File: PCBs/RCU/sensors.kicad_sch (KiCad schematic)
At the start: 10 parts

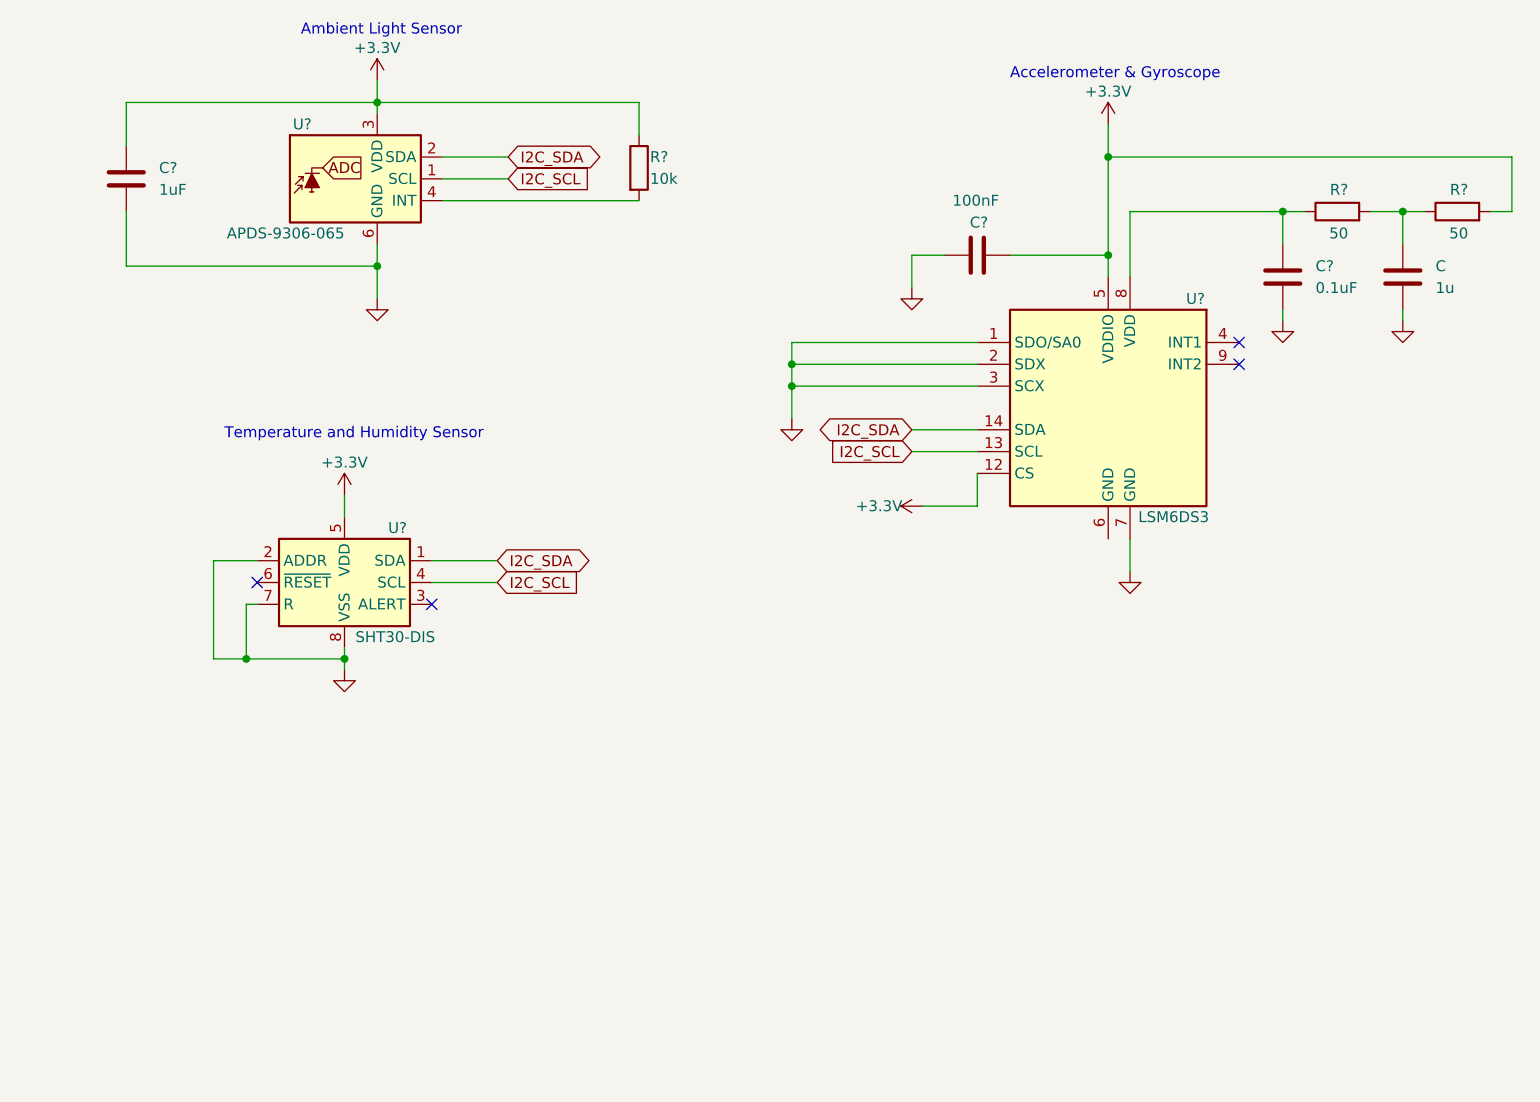
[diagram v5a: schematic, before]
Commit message: Numbered and ordered all of the modules
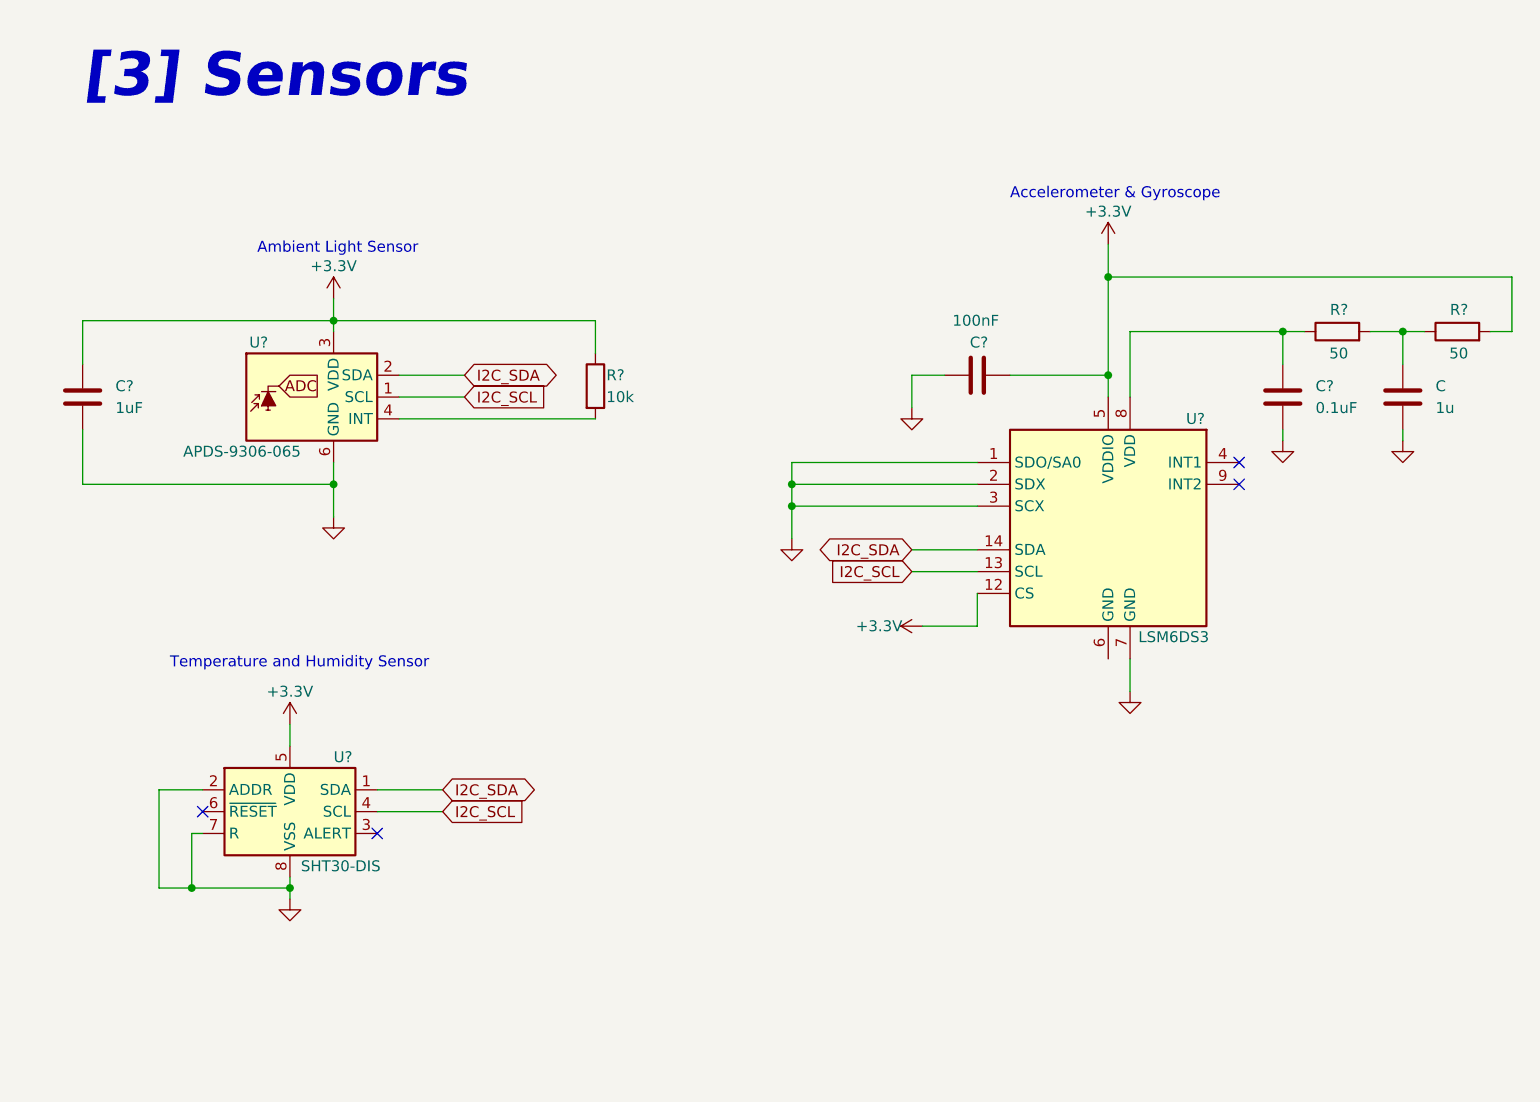
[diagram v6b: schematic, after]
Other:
- note added: "[3] Sensors"
- moved on the sheet: C, C?, R?, U?

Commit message: Annotated all components in sensors module
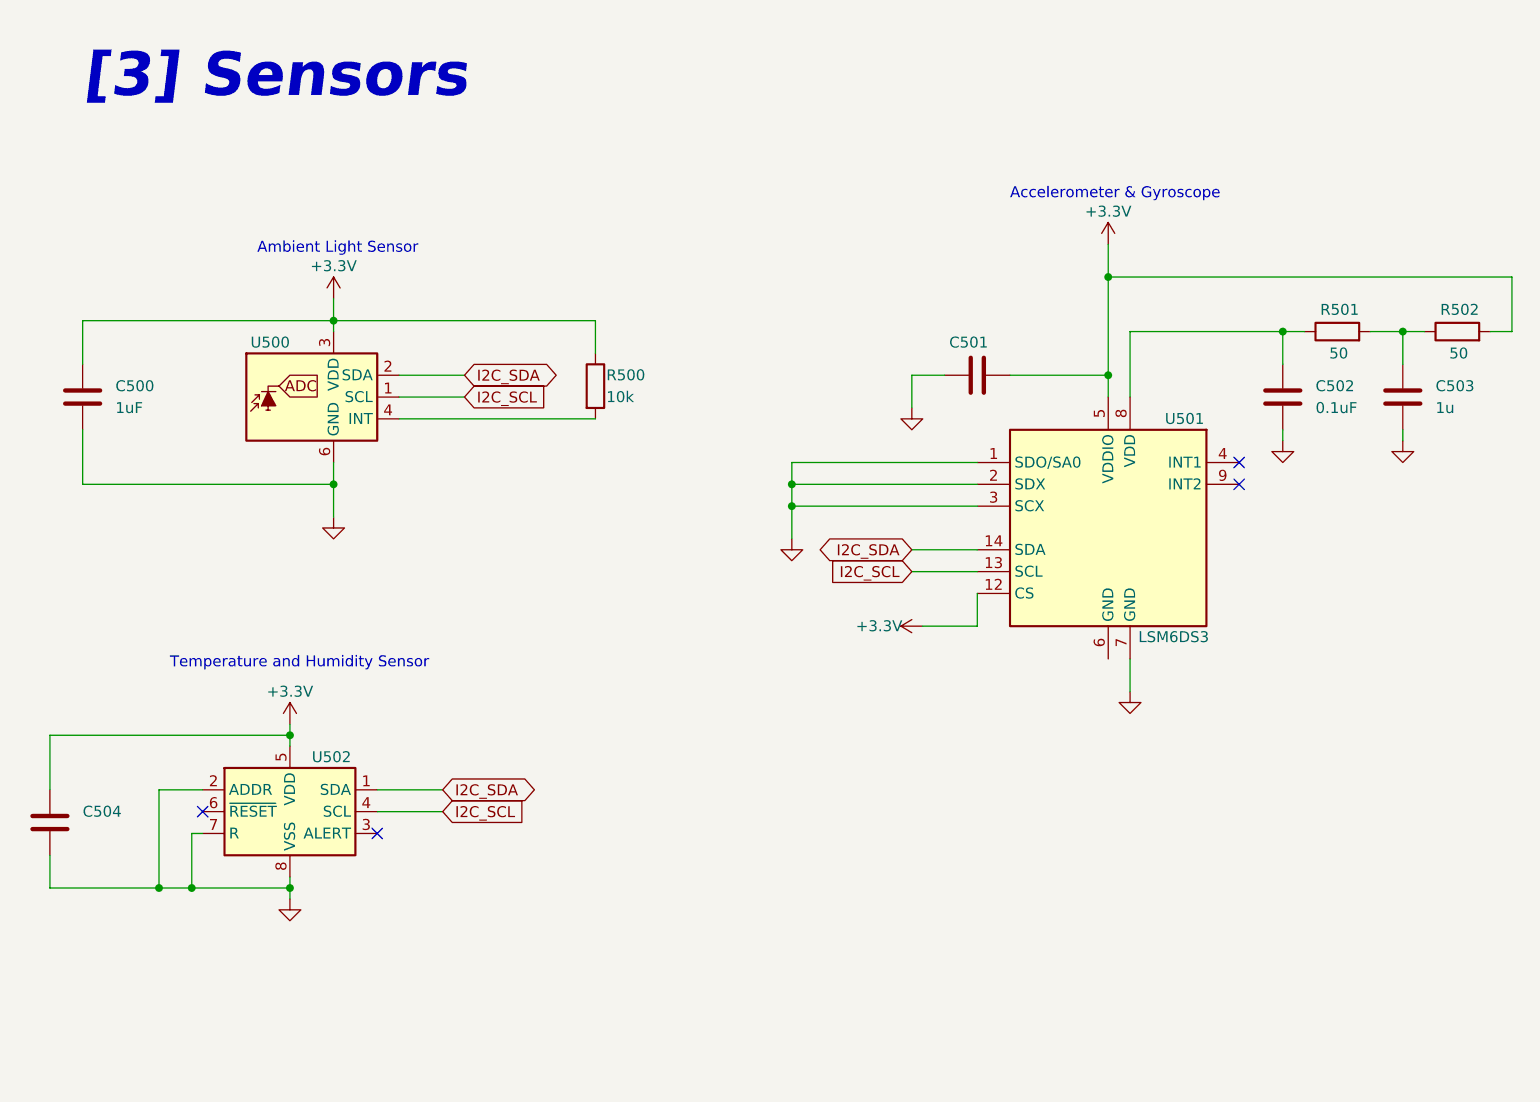
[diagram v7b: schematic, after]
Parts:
- added C504: (no value), symbol Device:C
- C501: renamed from C?; value 100nF -> (none)
- U500: renamed from U?; value APDS-9306-065 -> (none); footprint OptoDevice:Broadcom_DFN-6_2x2mm_P0.65mm -> (none)
- U502: renamed from U?; value SHT30-DIS -> (none); footprint Sensor_Humidity:Sensirion_DFN-8-1EP_2.5x2.5mm_P0.5mm_EP1.1x1.7mm -> (none)
- gave numbers to parts that had none: 6
- renumbered C to C503
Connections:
- net +3V3: now also C504.1
- net GND: now also C504.2
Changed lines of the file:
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@@
 (kicad_sch (version 20211123) (generator eeschema)
   (paper "A5")
+  (junction (at 30.48 119.38) (diameter 0) (color 0 0 0 0)
+  )
   (junction (at 140.97 59.69) (diameter 0) (color 0 0 0 0)
   )
@@
   )
   (junction (at 50.8 53.34) (diameter 0) (color 0 0 0 0)
+  )
+  (junction (at 45.72 101.6) (diameter 0) (color 0 0 0 0)
   )
   (junction (at 161.29 54.61) (diameter 0) (color 0 0 0 0)
@@
     (stroke (width 0) (type default) (color 0 0 0 0))
   )
+  (wire (pts (xy 45.72 101.6) (xy 45.72 102.87))
+    (stroke (width 0) (type default) (color 0 0 0 0))
+  )
   (wire (pts (xy 21.59 53.34) (xy 21.59 58.42))
     (stroke (width 0) (type default) (color 0 0 0 0))
@@
     (stroke (width 0) (type default) (color 0 0 0 0))
   )
+  (wire (pts (xy 17.78 119.38) (xy 30.48 119.38))
+    (stroke (width 0) (type default) (color 0 0 0 0))
+  )
   (wire (pts (xy 143.51 92.71) (xy 143.51 96.52))
     (stroke (width 0) (type default) (color 0 0 0 0))
@@
     (stroke (width 0) (type default) (color 0 0 0 0))
   )
+  (wire (pts (xy 17.78 115.57) (xy 17.78 119.38))
+    (stroke (width 0) (type default) (color 0 0 0 0))
+  )
   (wire (pts (xy 21.59 66.04) (xy 21.59 72.39))
     (stroke (width 0) (type default) (color 0 0 0 0))
@@
     (stroke (width 0) (type default) (color 0 0 0 0))
   )
+  (wire (pts (xy 17.78 107.95) (xy 17.78 101.6))
+    (stroke (width 0) (type default) (color 0 0 0 0))
+  )
   (wire (pts (xy 143.51 62.23) (xy 143.51 54.61))
     (stroke (width 0) (type default) (color 0 0 0 0))
@@
     (stroke (width 0) (type default) (color 0 0 0 0))
   )
-  (wire (pts (xy 45.72 100.33) (xy 45.72 102.87))
+  (wire (pts (xy 45.72 100.33) (xy 45.72 101.6))
     (stroke (width 0) (type default) (color 0 0 0 0))
   )
@@
   )
   (wire (pts (xy 125.73 85.09) (xy 125.73 88.9))
+    (stroke (width 0) (type default) (color 0 0 0 0))
+  )
+  (wire (pts (xy 17.78 101.6) (xy 45.72 101.6))
     (stroke (width 0) (type default) (color 0 0 0 0))
   )
@@
   (symbol (lib_id "Device:C") (at 21.59 62.23 0) (unit 1)
     (in_bom yes) (on_board yes) (fields_autoplaced)
-    (property "Reference" "C?" (id 0) (at 25.4 60.9599 0)
+    (property "Reference" "C500" (id 0) (at 25.4 60.9599 0)
       (effects (font (size 1.27 1.27)) (justify left))
     )
@@
   (symbol (lib_id "Sensor_Humidity:SHT30-DIS") (at 45.72 110.49 0) (unit 1)
     (in_bom yes) (on_board yes)
-    (property "Reference" "U?" (id 0) (at 50.8 104.14 0)
-      (effects (font (size 1.27 1.27)) (justify left))
-    )
-    (property "Value" "SHT30-DIS" (id 1) (at 46.99 116.84 0)
-      (effects (font (size 1.27 1.27)) (justify left))
-    )
-    (property "Footprint" "Sensor_Humidity:Sensirion_DFN-8-1EP_2.5x2.5mm_P0.5mm_EP1.1x1.7mm" (id 2) (at 45.72 109.22 0)
+    (property "Reference" "U502" (id 0) (at 48.26 104.14 0)
+      (effects (font (size 1.27 1.27)) (justify left))
+    )
+    (property "Value" "" (id 1) (at 46.99 116.84 0)
+      (effects (font (size 1.27 1.27)) (justify left))
+    )
+    (property "Footprint" "" (id 2) (at 45.72 109.22 0)
       (effects (font (size 1.27 1.27)) hide)
     )
@@
   (symbol (lib_id "Device:R") (at 81.28 60.96 0) (unit 1)
     (in_bom yes) (on_board yes)
-    (property "Reference" "R?" (id 0) (at 82.55 59.69 0)
+    (property "Reference" "R500" (id 0) (at 82.55 59.69 0)
       (effects (font (size 1.27 1.27)) (justify left))
     )
@@
   (symbol (lib_id "Sensor_Optical:APDS-9306-065") (at 48.26 62.23 0) (unit 1)
     (in_bom yes) (on_board yes)
-    (property "Reference" "U?" (id 0) (at 43.18 55.88 0)
+    (property "Reference" "U500" (id 0) (at 45.72 55.88 0)
       (effects (font (size 1.27 1.27)) (justify right))
     )
-    (property "Value" "APDS-9306-065" (id 1) (at 46.99 68.58 0)
+    (property "Value" "" (id 1) (at 46.99 68.58 0)
       (effects (font (size 1.27 1.27)) (justify right))
     )
-    (property "Footprint" "OptoDevice:Broadcom_DFN-6_2x2mm_P0.65mm" (id 2) (at 48.26 74.93 0)
+    (property "Footprint" "" (id 2) (at 48.26 74.93 0)
       (effects (font (size 1.27 1.27)) hide)
     )
@@
     (pin "6")
   )
+  (symbol (lib_id "Device:C") (at 17.78 111.76 0) (unit 1)
+    (in_bom yes) (on_board yes) (fields_autoplaced)
+    (property "Reference" "C504" (id 0) (at 21.59 110.4899 0)
+      (effects (font (size 1.27 1.27)) (justify left))
+    )
+    (property "Value" "" (id 1) (at 21.59 113.0299 0)
+      (effects (font (size 1.27 1.27)) (justify left))
+    )
+    (property "Footprint" "" (id 2) (at 18.7452 115.57 0)
+      (effects (font (size 1.27 1.27)) hide)
+    )
+    (property "Datasheet" "~" (id 3) (at 17.78 111.76 0)
+      (effects (font (size 1.27 1.27)) hide)
+    )
+    (pin "1")
+    (pin "2")
+  )
   (symbol (lib_id "Device:C") (at 161.29 62.23 180) (unit 1)
     (in_bom yes) (on_board yes) (fields_autoplaced)
-    (property "Reference" "C?" (id 0) (at 165.1 60.9599 0)
+    (property "Reference" "C502" (id 0) (at 165.1 60.9599 0)
       (effects (font (size 1.27 1.27)) (justify right))
     )
@@
   (symbol (lib_id "Device:R") (at 167.64 54.61 90) (unit 1)
     (in_bom yes) (on_board yes)
-    (property "Reference" "R?" (id 0) (at 168.91 52.07 90)
+    (property "Reference" "R501" (id 0) (at 170.18 52.07 90)
       (effects (font (size 1.27 1.27)) (justify left))
     )
@@
   (symbol (lib_id "Device:C") (at 175.26 62.23 180) (unit 1)
     (in_bom yes) (on_board yes) (fields_autoplaced)
-    (property "Reference" "C" (id 0) (at 179.07 60.9599 0)
+    (property "Reference" "C503" (id 0) (at 179.07 60.9599 0)
       (effects (font (size 1.27 1.27)) (justify right))
     )
@@
   (symbol (lib_id "Device:R") (at 181.61 54.61 90) (unit 1)
     (in_bom yes) (on_board yes)
-    (property "Reference" "R?" (id 0) (at 182.88 52.07 90)
+    (property "Reference" "R502" (id 0) (at 184.15 52.07 90)
       (effects (font (size 1.27 1.27)) (justify left))
     )
@@
   (symbol (lib_id "Sensor_Motion:LSM6DS3") (at 140.97 77.47 0) (unit 1)
     (in_bom yes) (on_board yes)
-    (property "Reference" "U?" (id 0) (at 151.13 64.77 0))
+    (property "Reference" "U501" (id 0) (at 149.86 64.77 0))
     (property "Value" "LSM6DS3" (id 1) (at 148.59 90.17 0))
     (property "Footprint" "Package_LGA:LGA-14_3x2.5mm_P0.5mm_LayoutBorder3x4y" (id 2) (at 130.81 95.25 0)
@@
   (symbol (lib_id "Device:C") (at 125.73 59.69 90) (unit 1)
     (in_bom yes) (on_board yes)
-    (property "Reference" "C?" (id 0) (at 127 55.88 90)
-      (effects (font (size 1.27 1.27)) (justify left))
-    )
-    (property "Value" "100nF" (id 1) (at 128.27 53.34 90)
-      (effects (font (size 1.27 1.27)) (justify left))
-    )
+    (property "Reference" "C501" (id 0) (at 127 55.88 90)
+      (effects (font (size 1.27 1.27)) (justify left))
+    )
+    (property "Value" "" (id 1) (at 127 63.5 90)
+      (effects (font (size 1.27 1.27)) (justify left))
+    )
